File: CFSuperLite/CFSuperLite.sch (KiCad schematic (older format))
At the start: 23 parts, among them J1 IDE_CONNECTOR, J2 CF Adapter Power, J3 Bus_ISA_8bit, J4 Addresses, J5 Addresses, U1 BIOS FLASH, U2 74HCT245, U3 ATF/GAL22V10x-15, U4 DS1315, U5 AS6C4008-55PCN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

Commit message: CFSuperLite: Mostly schematic work to direct-connect the SST flash to bus. Remove now-redundant signals from the glue and switch to a smaller 16V8 GAL. Layout needs to be redone. Should change some component selections first.
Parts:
- removed U3: ATF/GAL22V10x-15, Package_DIP:DIP-24_W7.62mm_Socket, symbol 00Common:GAL22V10
- removed U5: AS6C4008-55PCN, Package_DIP:DIP-32_W15.24mm_Socket, symbol Memory_RAM:AS6C4008-55PCN
- added U3: ATF/GAL16V8x-15, Package_DIP:DIP-20_W7.62mm_Socket, symbol 00Common:GAL16V8
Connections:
- net ~IOR_OR_MEMR is gone; now on net ~IOR: U2.1 (A->B)
- net ~IOR~_DELAYED is gone; now on net ~IOR: J1.25 (~IOR)
- net ~MEMR~_DELAYED is gone; now on net ~MEMR: U1.24 (OE), U4.12 (~OE)
- net A04: now also U3.1 (I1/CLK)
- net A05: now also U3.2 (I2)
- net A06: now also U3.3 (I3)
- net A07: now also U3.4 (I4)
- net A08: now also U3.5 (I5)
- net A09: now also U3.6 (I6)
- net A15: now also U3.8 (I8)
- net A16: now also U3.9 (I9)
- net A17: now also U3.11 (I10/~OE~)
- net A18: now also U3.12 (IO8)
- net A19: now also U3.13 (IO7)
- net ATA_ADDR_JUMPER: now also U3.18 (IO2)
- net D0: now also U1.13 (D0)
- net D0_BUF: no longer U1.13 (D0)
- net D1: now also U1.14 (D1)
- net D1_BUF: no longer U1.14 (D1)
- net D2: now also U1.15 (D2)
- net D2_BUF: no longer U1.15 (D2)
- net D3: now also U1.17 (D3)
- net D3_BUF: no longer U1.17 (D3)
- net D4: now also U1.18 (D4)
- net D4_BUF: no longer U1.18 (D4)
- net D5: now also U1.19 (D5)
- net D5_BUF: no longer U1.19 (D5)
- net D6: now also U1.20 (D6)
- net D6_BUF: no longer U1.20 (D6)
- net D7: now also U1.21 (D7)
- net D7_BUF: no longer U1.21 (D7)
- net GND: now also U3.10 (GND); no longer U2.19 (CE)
- net RESET: now also U3.7 (I7)
- net ROM_ADDR_JUMPER: now also U3.19 (IO1)
- net VCC: now also U3.20 (VCC)
- net ~CE~_BIOS_DECODE: now also U3.14 (IO6)
- net ~CS1~_ATA: now also U2.19 (CE), U3.15 (IO5)
- net ~RESET: now also U3.16 (IO4)
- net AEN: now reaches J3.42 (AEN)
- net AEN: now also U3.17 (I03)
- no-connect marks 39 -> 38
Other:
- note removed: "TANDY 1000 SRAM\n(OPTIONAL)"
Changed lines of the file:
@@
 	8550 1850 9150 1850
 Text GLabel 9150 2150 0    39   Input ~ 0
-~IOR~_DELAYED
+~IOR
 Text GLabel 9150 2050 0    39   Input ~ 0
 ~IOW
@@
 L power:GND #PWR0110
 U 1 1 60418ECC
-P 4450 2500
-F 0 "#PWR0110" H 4450 2250 50  0001 C CNN
-F 1 "GND" H 4455 2327 50  0000 C CNN
-F 2 "" H 4450 2500 50  0001 C CNN
-F 3 "" H 4450 2500 50  0001 C CNN
-	1    4450 2500
+P 4450 2400
+F 0 "#PWR0110" H 4450 2150 50  0001 C CNN
+F 1 "GND" H 4455 2227 50  0000 C CNN
+F 2 "" H 4450 2400 50  0001 C CNN
+F 3 "" H 4450 2400 50  0001 C CNN
+	1    4450 2400
 	1    0    0    -1
 $EndComp
@@
 ~MEMW
 Text GLabel 6700 5900 0    39   Input ~ 0
-~MEMR~_DELAYED
+~MEMR
 Text GLabel 6700 5800 0    39   Input ~ 0
 ~CE~_BIOS
-Text GLabel 7900 3600 2    50   Input ~ 0
-D0_BUF
-Text GLabel 7900 3700 2    50   Input ~ 0
-D1_BUF
-Text GLabel 7900 3800 2    50   Input ~ 0
-D2_BUF
-Text GLabel 7900 3900 2    50   Input ~ 0
-D3_BUF
-Text GLabel 7900 4000 2    50   Input ~ 0
-D4_BUF
-Text GLabel 7900 4100 2    50   Input ~ 0
-D5_BUF
-Text GLabel 7900 4200 2    50   Input ~ 0
-D6_BUF
-Text GLabel 7900 4300 2    50   Input ~ 0
-D7_BUF
 Text GLabel 4950 1600 2    39   Input ~ 0
 ~CS1~_ATA
 Text GLabel 4950 1700 2    39   Input ~ 0
 ~CE~_BIOS_DECODE
-Text GLabel 4950 2100 2    39   Input ~ 0
-~IOR~_DELAYED
 Text GLabel 2600 3400 2    50   Input ~ 0
 A06
@@
 Text GLabel 2600 2500 2    50   Input ~ 0
 A15
-Text GLabel 3950 2300 0    50   Input ~ 0
+Text GLabel 4950 1800 2    50   Input ~ 0
 A19
-Text GLabel 3950 2200 0    50   Input ~ 0
+Text GLabel 4950 1900 2    50   Input ~ 0
 A18
 Text GLabel 3950 2100 0    50   Input ~ 0
@@
 NoConn ~ 1500 3600
 NoConn ~ 1500 2900
-NoConn ~ 2500 2000
 NoConn ~ 1500 1400
 NoConn ~ 1500 1600
@@
 D0
 Text GLabel 4150 4750 0    39   Input ~ 0
-~IOR_OR_MEMR
+~IOR
 Text GLabel 4950 1200 2    50   Input ~ 0
 ROM_ADDR_JUMPER
 Text GLabel 4950 1300 2    50   Input ~ 0
 ATA_ADDR_JUMPER
-$Comp
-L 00Common:GAL22V10 U3
-U 1 1 604CA5F0
-P 4450 1700
-F 0 "U3" H 4650 2450 50  0000 C CNN
-F 1 "ATF/GAL22V10x-15" H 4900 2350 50  0000 C CNN
-F 2 "Package_DIP:DIP-24_W7.62mm_Socket" H 4450 1700 50  0001 C CNN
-F 3 "" H 4450 1700 50  0001 C CNN
-	1    4450 1700
-	1    0    0    -1
-$EndComp
 Text GLabel 2600 2600 2    50   Input ~ 0
 A14
@@
 Text GLabel 3950 1800 0    50   Input ~ 0
 RESET
-Text GLabel 4950 1800 2    39   Input ~ 0
-~MEMR
 $Comp
 L 00Common:Bus_ISA_8bit J3
@@
 	3800 6600 4100 6600
 Text GLabel 4100 6600 2    39   Input ~ 0
-~MEMR~_DELAYED
+~MEMR
 $Comp
 L power:GND #PWR0127
@@
 Text Notes 600  6000 0    79   ~ 0
 REAL TIME CLOCK\n(OPTIONAL)
-$Comp
-L Memory_RAM:AS6C4008-55PCN U5
-U 1 1 605402C7
-P 9700 5000
-F 0 "U5" H 9850 6150 50  0000 C CNN
-F 1 "AS6C4008-55PCN" H 10150 6050 50  0000 C CNN
-F 2 "Package_DIP:DIP-32_W15.24mm_Socket" H 9700 5100 50  0001 C CNN
-F 3 "https://www.alliancememory.com/wp-content/uploads/pdf/AS6C4008.pdf" H 9700 5100 50  0001 C CNN
-	1    9700 5000
-	1    0    0    -1
-$EndComp
-Text GLabel 9200 4100 0    50   Input ~ 0
-A00
-Text GLabel 9200 4200 0    50   Input ~ 0
-A01
-Text GLabel 9200 4300 0    50   Input ~ 0
-A02
-Text GLabel 9200 4400 0    50   Input ~ 0
-A03
-Text GLabel 9200 4500 0    50   Input ~ 0
-A04
-Text GLabel 9200 4600 0    50   Input ~ 0
-A05
-Text GLabel 9200 4700 0    50   Input ~ 0
-A06
-Text GLabel 9200 4800 0    50   Input ~ 0
-A07
-Text GLabel 9200 4900 0    50   Input ~ 0
-A08
-Text GLabel 9200 5000 0    50   Input ~ 0
-A09
-Text GLabel 9200 5100 0    50   Input ~ 0
-A10
-Text GLabel 9200 5200 0    50   Input ~ 0
-A11
-Text GLabel 9200 5300 0    50   Input ~ 0
-A12
-Text GLabel 9200 5400 0    50   Input ~ 0
-A13
-Text GLabel 9200 5500 0    50   Input ~ 0
-A14
-Text GLabel 9200 5900 0    50   Input ~ 0
-A18
-Text GLabel 9200 5800 0    50   Input ~ 0
-A17
-Text GLabel 9200 5700 0    50   Input ~ 0
-A16
-Text GLabel 9200 5600 0    50   Input ~ 0
-A15
-Text GLabel 10200 4100 2    50   Input ~ 0
-D0_BUF
-Text GLabel 10200 4200 2    50   Input ~ 0
-D1_BUF
-Text GLabel 10200 4300 2    50   Input ~ 0
-D2_BUF
-Text GLabel 10200 4400 2    50   Input ~ 0
-D3_BUF
-Text GLabel 10200 4500 2    50   Input ~ 0
-D4_BUF
-Text GLabel 10200 4600 2    50   Input ~ 0
-D5_BUF
-Text GLabel 10200 4700 2    50   Input ~ 0
-D6_BUF
-Text GLabel 10200 4800 2    50   Input ~ 0
-D7_BUF
-Text GLabel 10200 5100 2    50   Input ~ 0
-A19
-Text GLabel 10200 5200 2    39   Input ~ 0
-~MEMR~_DELAYED
-Text GLabel 10200 5300 2    39   Input ~ 0
-~MEMW
-Text Notes 8500 3750 0    79   ~ 0
-TANDY 1000 SRAM\n(OPTIONAL)
-Wire Notes Line
-	8450 3450 11150 3450
-Wire Notes Line
-	11150 3450 11150 6450
-Wire Notes Line
-	11150 6450 8450 6450
-Wire Notes Line
-	8450 6450 8450 3450
-$Comp
-L power:GND #PWR0130
-U 1 1 60513BF2
-P 9700 6100
-F 0 "#PWR0130" H 9700 5850 50  0001 C CNN
-F 1 "GND" H 9705 5927 50  0000 C CNN
-F 2 "" H 9700 6100 50  0001 C CNN
-F 3 "" H 9700 6100 50  0001 C CNN
-	1    9700 6100
-	1    0    0    -1
-$EndComp
-$Comp
-L power:VCC #PWR0131
-U 1 1 60514347
-P 9700 3900
-F 0 "#PWR0131" H 9700 3750 50  0001 C CNN
-F 1 "VCC" H 9715 4073 50  0000 C CNN
-F 2 "" H 9700 3900 50  0001 C CNN
-F 3 "" H 9700 3900 50  0001 C CNN
-	1    9700 3900
-	1    0    0    -1
-$EndComp
 $Comp
 L power:VCC #PWR0132
@@
 	1    0    0    -1
 $EndComp
-Text GLabel 4950 2000 2    39   Input ~ 0
-~IOR_OR_MEMR
 Text GLabel 4950 1500 2    39   Input ~ 0
 ~RESET
-Text GLabel 4950 1400 2    39   Input ~ 0
-~IOR
 Wire Notes Line
 	5900 2950 5900 550
@@
 Wire Wire Line
 	10500 1700 10500 1900
-Text GLabel 4950 1900 2    39   Input ~ 0
-~MEMR~_DELAYED
-$Comp
-L power:GND #PWR0134
-U 1 1 60C19D5B
-P 4050 5150
-F 0 "#PWR0134" H 4050 4900 50  0001 C CNN
-F 1 "GND" H 4055 4977 50  0000 C CNN
-F 2 "" H 4050 5150 50  0001 C CNN
-F 3 "" H 4050 5150 50  0001 C CNN
-	1    4050 5150
-	1    0    0    -1
-$EndComp
-Wire Wire Line
-	4150 4850 4050 4850
-Wire Wire Line
-	4050 4850 4050 5150
 Text GLabel 6700 5000 0    50   Input ~ 0
 A14
@@
 Text GLabel 6700 5200 0    50   Input ~ 0
 V20_JUMPER
+Text GLabel 7900 4300 2    50   Input ~ 0
+D7
+Text GLabel 7900 4200 2    50   Input ~ 0
+D6
+Text GLabel 7900 4100 2    50   Input ~ 0
+D5
+Text GLabel 7900 4000 2    50   Input ~ 0
+D4
+Text GLabel 7900 3900 2    50   Input ~ 0
+D3
+Text GLabel 7900 3800 2    50   Input ~ 0
+D2
+Text GLabel 7900 3700 2    50   Input ~ 0
+D1
+Text GLabel 7900 3600 2    50   Input ~ 0
+D0
+$Comp
+L 00Common:GAL16V8 U3
+U 1 1 615ED28D
+P 4450 1700
+F 0 "U3" H 4650 2450 50  0000 C CNN
+F 1 "ATF/GAL16V8x-15" H 4850 2350 50  0000 C CNN
+F 2 "Package_DIP:DIP-20_W7.62mm_Socket" H 4450 1700 50  0001 C CNN
+F 3 "http://www.ti.com/lit/gpn/sn74LS245" H 4450 1700 50  0001 C CNN
+	1    4450 1700
+	1    0    0    -1
+$EndComp
+Text GLabel 4950 1400 2    50   Input ~ 0
+AEN
+Text GLabel 4150 4850 0    39   Input ~ 0
+~CS1~_ATA
+Text GLabel 2500 2000 2    50   Input ~ 0
+AEN
 $EndSCHEMATC

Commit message: WIP on CFSuperLite layout. Switched it to use a dip switch rather than jumpers.
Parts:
- removed J4, J5: Addresses, Connector_PinHeader_2.54mm:PinHeader_2x03_P2.54mm_Vertical, symbol Connector_Generic:Conn_02x03_Odd_Even
- added R1, R2, R3: 10K, Resistor_SMD:R_1206_3216Metric, symbol Device:R
- added SW1: Options, Button_Switch_THT:SW_DIP_SPSTx04_Slide_9.78x12.34mm_W7.62mm_P2.54mm, symbol Switch:SW_DIP_x04
- C1, C2, C3, C4, C5, C6: footprint Capacitor_THT:C_Disc_D6.0mm_W2.5mm_P5.00mm -> Capacitor_SMD:C_1206_3216Metric; LCSC C84772 -> C24497; Part options C84772,C263183 -> (none)
- C7: value 22uF -> 22uF-33uF 16-25v; footprint Capacitor_THT:CP_Radial_D5.0mm_P2.50mm -> Capacitor_Tantalum_SMD:CP_EIA-3528-15_AVX-H; LCSC (none) -> C10785; Part options (none) -> C10785, C125779, C139576
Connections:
- net ~CE~_BIOS is gone; now on net ~CE~_BIOS_THRU: U1.22 (CE)
- net A15: now also U3.13 (IO7); no longer U3.8 (I8)
- net A16: now also U3.8 (I8); no longer U3.9 (I9)
- net A17: now also U3.12 (IO8); no longer U3.11 (I10/~OE~)
- net A18: now also U3.9 (I9); no longer U3.12 (IO8)
- net A19: now also U3.11 (I10/~OE~); no longer U3.13 (IO7)
- net ATA_ADDR_JUMPER: now also R2.2, SW1.7
- net GND: now also SW1.1, SW1.2, SW1.3
- net ROM_ADDR_JUMPER: now also R1.2, SW1.8
- net V20_JUMPER: now also R3.2, SW1.6
- net VCC: now also R1.1, R2.1, R3.1
- net ~CE~_BIOS_DECODE: now also SW1.4
- net ~CE~_BIOS_THRU: now also SW1.5; no longer U4.10 (~CEO)

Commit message: CFSuperLite WIP.
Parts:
- removed C5: 0.1uF, Capacitor_SMD:C_1206_3216Metric, symbol Device:C
- renumbered C6 to C5, C7 to C6
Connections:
- net A04: now also U3.8 (I8); no longer U3.1 (I1/CLK)
- net A05: now also U3.13 (IO7); no longer U3.2 (I2)
- net A06: now also U3.5 (I5); no longer U3.3 (I3)
- net A08: now also U3.6 (I6); no longer U3.5 (I5)
- net A09: now also U3.7 (I7); no longer U3.6 (I6)
- net A15: now also U3.3 (I3); no longer U3.13 (IO7)
- net A16: now also U3.1 (I1/CLK); no longer U3.8 (I8)
- net A18: now also U3.2 (I2); no longer U3.9 (I9)
- net ATA_ADDR_JUMPER: now also U3.19 (IO1); no longer U3.18 (IO2)
- net D0: now also U4.7 (Q)
- net D0_BUF: no longer U4.7 (Q)
- net RESET: now also U3.9 (I9); no longer U3.7 (I7)
- net ROM_ADDR_JUMPER: now also U3.18 (IO2); no longer U3.19 (IO1)
- net XTAL1: now also Y1.2; no longer Y1.1
- net XTAL2: now also Y1.1; no longer Y1.2
- net ~CE~_BIOS_THRU: now also U4.10 (~CEO)
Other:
- moved on the sheet: C5, C6
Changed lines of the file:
@@
 Text GLabel 3950 1500 0    50   Input ~ 0
 A07
-Text GLabel 3950 1600 0    50   Input ~ 0
+Text GLabel 3950 1700 0    50   Input ~ 0
 A08
-Text GLabel 3950 1700 0    50   Input ~ 0
+Text GLabel 3950 1800 0    50   Input ~ 0
 A09
-Text GLabel 3950 1400 0    50   Input ~ 0
-A06
-Text GLabel 3950 1300 0    50   Input ~ 0
-A05
-Text GLabel 3950 1200 0    50   Input ~ 0
+Text GLabel 3950 1900 0    50   Input ~ 0
 A04
 Text GLabel 2600 2100 2    50   Input ~ 0
@@
 Text GLabel 3950 2100 0    50   Input ~ 0
 A19
-Text GLabel 3950 2000 0    50   Input ~ 0
+Text GLabel 3950 1300 0    50   Input ~ 0
 A18
-Text GLabel 4950 1900 2    50   Input ~ 0
-A17
-Text GLabel 3950 1900 0    50   Input ~ 0
+Text GLabel 3950 1200 0    50   Input ~ 0
 A16
-Text GLabel 4950 1800 2    50   Input ~ 0
-A15
 Connection ~ 6100 5400
 Wire Wire Line
@@
 Text GLabel 4150 4750 0    39   Input ~ 0
 ~IOR
+Text GLabel 4950 1300 2    50   Input ~ 0
+ROM_ADDR_JUMPER
 Text GLabel 4950 1200 2    50   Input ~ 0
-ROM_ADDR_JUMPER
-Text GLabel 4950 1300 2    50   Input ~ 0
 ATA_ADDR_JUMPER
 Text GLabel 2600 2600 2    50   Input ~ 0
@@
 Wire Wire Line
 	2500 2600 2600 2600
-Text GLabel 3950 1800 0    50   Input ~ 0
+Text GLabel 3950 2000 0    50   Input ~ 0
 RESET
 $Comp
@@
 F 3 "~" H 1800 6050 50  0001 C CNN
 	1    1800 6050
-	0    1    1    0
+	0    1    -1   0
 $EndComp
 Wire Wire Line
@@
 	3800 6300 3900 6300
 Text GLabel 2650 6800 0    50   Input ~ 0
-D0_BUF
+D0
 Text GLabel 2650 6700 0    50   Input ~ 0
 A00
@@
 REAL TIME CLOCK\n(OPTIONAL)
 $Comp
-L Device:CP C7
+L Device:CP C6
 U 1 1 60440B68
-P 6200 7050
-F 0 "C7" H 6318 7096 50  0000 L CNN
-F 1 "22uF-33uF 16-25v" V 6500 6650 50  0000 L CNN
-F 2 "Capacitor_Tantalum_SMD:CP_EIA-3528-15_AVX-H" H 6238 6900 50  0001 C CNN
-F 3 "~" H 6200 7050 50  0001 C CNN
-F 4 "C10785" H 6200 7050 50  0001 C CNN "LCSC"
-F 5 "C10785, C125779,  C139576" H 6200 7050 50  0001 C CNN "Part options"
-	1    6200 7050
-	1    0    0    -1
-$EndComp
-$Comp
-L power:VCC #PWR0122
-U 1 1 6043C274
-P 6200 6900
-F 0 "#PWR0122" H 6200 6750 50  0001 C CNN
-F 1 "VCC" H 6215 7073 50  0000 C CNN
-F 2 "" H 6200 6900 50  0001 C CNN
-F 3 "" H 6200 6900 50  0001 C CNN
-	1    6200 6900
-	1    0    0    -1
-$EndComp
-$Comp
-L power:GND #PWR0121
-U 1 1 6043C26A
-P 6200 7200
-F 0 "#PWR0121" H 6200 6950 50  0001 C CNN
-F 1 "GND" H 6205 7027 50  0000 C CNN
-F 2 "" H 6200 7200 50  0001 C CNN
-F 3 "" H 6200 7200 50  0001 C CNN
-	1    6200 7200
+P 3200 5150
+F 0 "C6" H 3318 5196 50  0000 L CNN
+F 1 "22uF-33uF 16-25v" V 3500 4750 50  0000 L CNN
+F 2 "Capacitor_Tantalum_SMD:CP_EIA-3528-15_AVX-H" H 3238 5000 50  0001 C CNN
+F 3 "~" H 3200 5150 50  0001 C CNN
+F 4 "C10785" H 3200 5150 50  0001 C CNN "LCSC"
+F 5 "C10785, C125779,  C139576" H 3200 5150 50  0001 C CNN "Part options"
+	1    3200 5150
 	1    0    0    -1
 $EndComp
@@
 $Comp
 L Device:C C5
-U 1 1 615EFBEE
+U 1 1 615EFEA0
 P 2700 5150
 F 0 "C5" H 2815 5196 50  0000 L CNN
@@
 F 5 "" H 2700 5150 50  0001 C CNN "Part options"
 	1    2700 5150
-	1    0    0    -1
-$EndComp
-$Comp
-L Device:C C6
-U 1 1 615EFEA0
-P 3200 5150
-F 0 "C6" H 3315 5196 50  0000 L CNN
-F 1 "0.1uF" H 3315 5105 50  0000 L CNN
-F 2 "Capacitor_SMD:C_1206_3216Metric" H 3238 5000 50  0001 C CNN
-F 3 "~" H 3200 5150 50  0001 C CNN
-F 4 " C24497" H 3200 5150 50  0001 C CNN "LCSC"
-F 5 "" H 3200 5150 50  0001 C CNN "Part options"
-	1    3200 5150
 	1    0    0    -1
 $EndComp
@@
 Wire Wire Line
 	6000 1700 6000 1800
+Text GLabel 4100 6800 2    39   Input ~ 0
+~CE~_BIOS_THRU
+Text GLabel 3950 1600 0    50   Input ~ 0
+A06
+Text GLabel 4950 1800 2    50   Input ~ 0
+A05
+Text GLabel 3950 1400 0    50   Input ~ 0
+A15
+Text GLabel 4950 1900 2    50   Input ~ 0
+A17
 $EndSCHEMATC

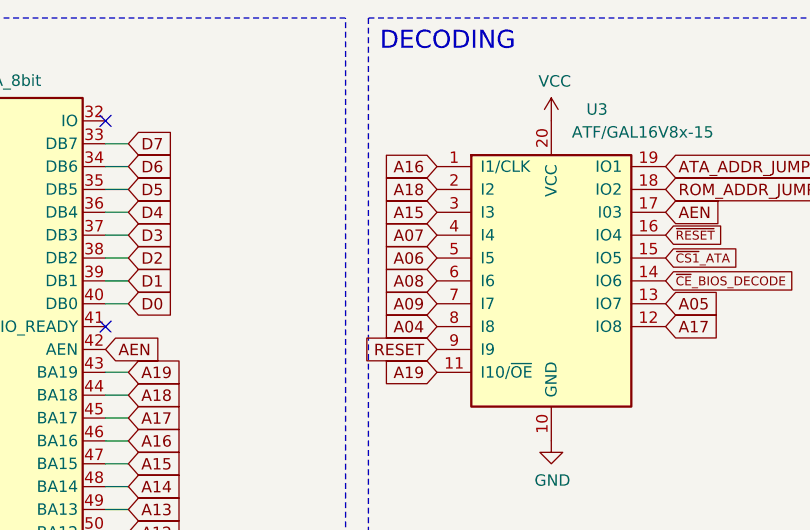
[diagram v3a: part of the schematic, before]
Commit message: CFSuperLite: DRC passing and all pads connected. Needs clean up.
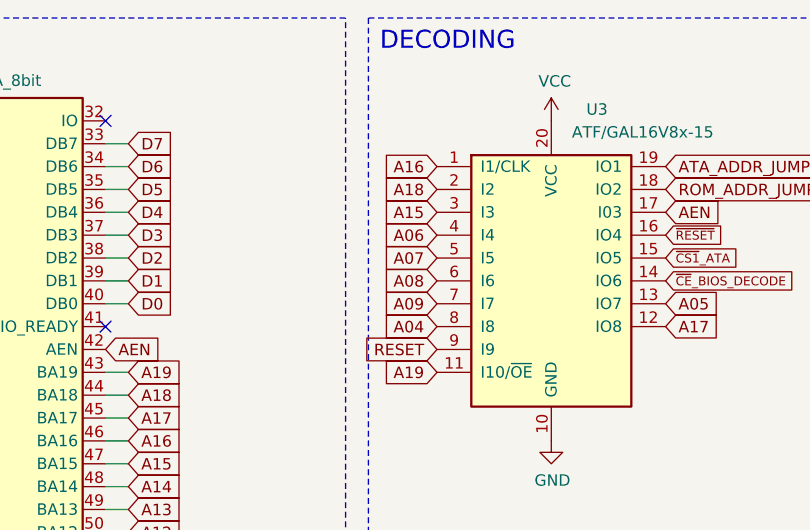
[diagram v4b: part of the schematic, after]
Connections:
- net A06: now also U3.4 (I4); no longer U3.5 (I5)
- net A07: now also U3.5 (I5); no longer U3.4 (I4)
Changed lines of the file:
@@
 Text GLabel 2600 3600 2    50   Input ~ 0
 A04
-Text GLabel 3950 1500 0    50   Input ~ 0
+Text GLabel 3950 1600 0    50   Input ~ 0
 A07
 Text GLabel 3950 1700 0    50   Input ~ 0
@@
 Text GLabel 4100 6800 2    39   Input ~ 0
 ~CE~_BIOS_THRU
-Text GLabel 3950 1600 0    50   Input ~ 0
+Text GLabel 3950 1500 0    50   Input ~ 0
 A06
 Text GLabel 4950 1800 2    50   Input ~ 0

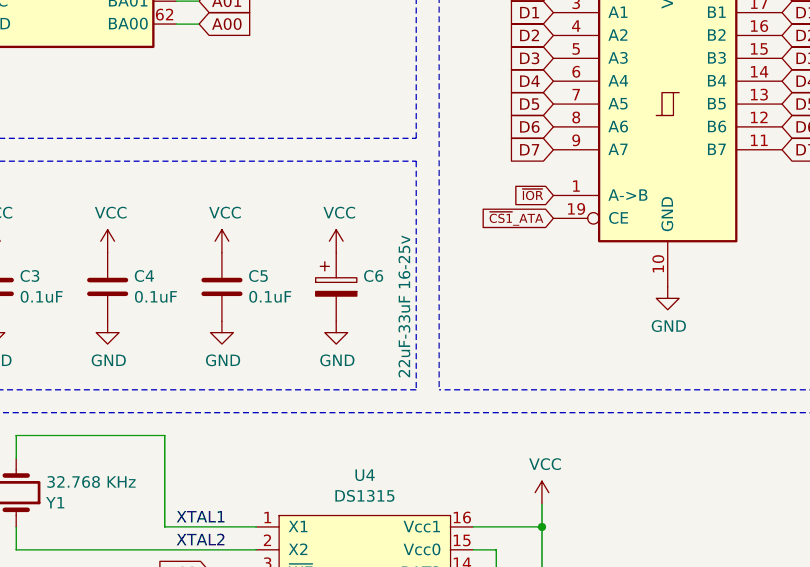
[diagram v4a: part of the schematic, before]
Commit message: CFSuperLite: Complete first pass on silkscreen. Board is complete.
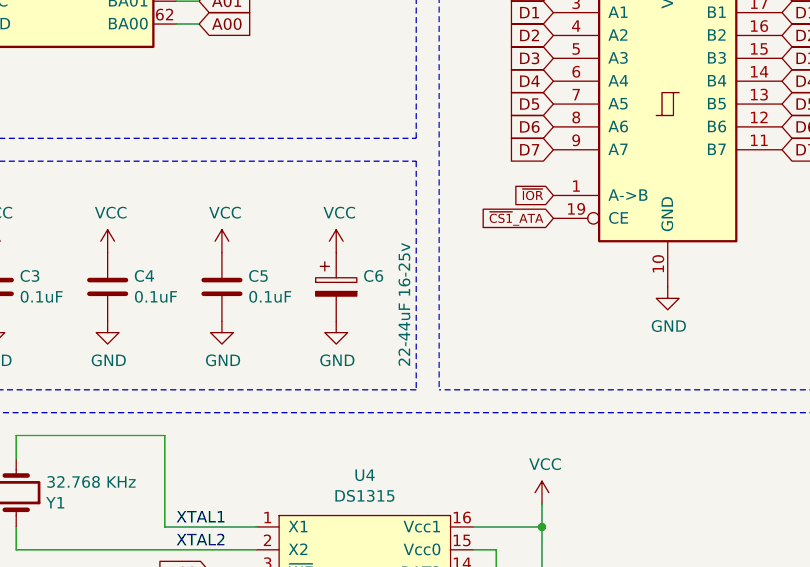
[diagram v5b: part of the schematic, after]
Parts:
- C6: value 22uF-33uF 16-25v -> 22-44uF 16-25v
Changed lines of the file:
@@
 P 3200 5150
 F 0 "C6" H 3318 5196 50  0000 L CNN
-F 1 "22uF-33uF 16-25v" V 3500 4750 50  0000 L CNN
+F 1 "22-44uF 16-25v" V 3500 4800 50  0000 L CNN
 F 2 "Capacitor_Tantalum_SMD:CP_EIA-3528-15_AVX-H" H 3238 5000 50  0001 C CNN
 F 3 "~" H 3200 5150 50  0001 C CNN

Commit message: Add remaining LCSC part numbers  to CFSuperLite symbols. Update bom file.
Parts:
- BAT1: LCSC (none) -> C964748; Part options (none) -> C964748, C964751, C964750
- J1: LCSC (none) -> C35165
- J2: LCSC (none) -> C225499; Part options (none) -> C225499, C49661
- SW1: LCSC (none) -> C15781; Part options (none) -> C15781, C99418, C319060, C47207
- U1: LCSC (none) -> C146583; Part options (none) -> C72122, C146583, C2331
- U2, U3: LCSC (none) -> C72118; Part options (none) -> C72118, C132507, C2328
- U4: LCSC (none) -> C72115; Part options (none) -> C72115, C146580, C2326
- Y1: LCSC (none) -> C127496
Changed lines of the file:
@@
 F 3 "http://ww1.microchip.com/downloads/en/DeviceDoc/25022B.pdf" H 7300 5100 50  0001 C CNN
 F 4 "SST39SF010, SST39SF020, SST39SF040 or similar" H 7300 6189 50  0000 C CNN "Note"
+F 5 "C146583" H 7300 4800 50  0001 C CNN "LCSC"
+F 6 "C72122, C146583, C2331" H 7300 4800 50  0001 C CNN "Part options"
 	1    7300 4800
 	1    0    0    -1
@@
 F 2 "Connector_PinSocket_2.54mm:PinSocket_2x20_P2.54mm_Vertical" H 9550 850 50  0001 C CNN
 F 3 "" H 9550 850 50  0001 C CNN
+F 4 "C35165" H 9550 850 50  0001 C CNN "LCSC"
 	1    9550 850
 	1    0    0    -1
@@
 F 2 "Connector_PinSocket_2.54mm:PinSocket_1x02_P2.54mm_Vertical" H 10750 950 50  0001 C CNN
 F 3 "~" H 10750 950 50  0001 C CNN
+F 4 "C225499" H 10750 950 50  0001 C CNN "LCSC"
+F 5 "C225499, C49661" H 10750 950 50  0001 C CNN "Part options"
 	1    10750 950
 	1    0    0    -1
@@
 F 2 "Package_DIP:DIP-20_W7.62mm_Socket" H 4650 4350 50  0001 C CNN
 F 3 "http://www.ti.com/lit/gpn/sn74LS245" H 4650 4350 50  0001 C CNN
+F 4 "C72118" H 4650 4350 50  0001 C CNN "LCSC"
+F 5 "C72118, C132507, C2328" H 4650 4350 50  0001 C CNN "Part options"
 	1    4650 4350
 	1    0    0    -1
@@
 F 2 "Battery:BatteryHolder_Keystone_103_1x20mm" V 1800 6860 50  0001 C CNN
 F 3 "~" V 1800 6860 50  0001 C CNN
+F 4 "C964748" H 1800 6800 50  0001 C CNN "LCSC"
+F 5 "C964748, C964751, C964750" H 1800 6800 50  0001 C CNN "Part options"
 	1    1800 6800
 	1    0    0    -1
@@
 F 2 "Crystal:Crystal_C38-LF_D3.0mm_L8.0mm_Horizontal" H 1800 6050 50  0001 C CNN
 F 3 "~" H 1800 6050 50  0001 C CNN
+F 4 "C127496" V 1800 6050 50  0001 C CNN "LCSC"
 	1    1800 6050
 	0    1    -1   0
@@
 F 2 "Package_DIP:DIP-16_W7.62mm_Socket" H 3300 6000 50  0001 C CNN
 F 3 "" H 3300 6000 50  0001 C CNN
+F 4 "C72115" H 3300 6000 50  0001 C CNN "LCSC"
+F 5 "C72115, C146580, C2326" H 3300 6000 50  0001 C CNN "Part options"
 	1    3300 6000
 	1    0    0    -1
@@
 F 2 "Package_DIP:DIP-20_W7.62mm_Socket" H 4450 1700 50  0001 C CNN
 F 3 "http://www.ti.com/lit/gpn/sn74LS245" H 4450 1700 50  0001 C CNN
+F 4 "C72118" H 4450 1700 50  0001 C CNN "LCSC"
+F 5 "C72118, C132507, C2328" H 4450 1700 50  0001 C CNN "Part options"
 	1    4450 1700
 	1    0    0    -1
@@
 F 2 "Button_Switch_THT:SW_DIP_SPSTx04_Slide_9.78x12.34mm_W7.62mm_P2.54mm" H 6600 1800 50  0001 C CNN
 F 3 "~" H 6600 1800 50  0001 C CNN
+F 4 "C15781" H 6600 1800 50  0001 C CNN "LCSC"
+F 5 "C15781, C99418, C319060, C47207" H 6600 1800 50  0001 C CNN "Part options"
 	1    6600 1800
 	1    0    0    -1
